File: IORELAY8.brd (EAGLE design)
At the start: 65 x 45 mm, 55 parts, among them Q1 2N7002, Q2 2N7002, Q3 2N7002, Q4 2N7002, Q5 2N7002, Q6 2N7002, Q7 2N7002, Q8 2N7002

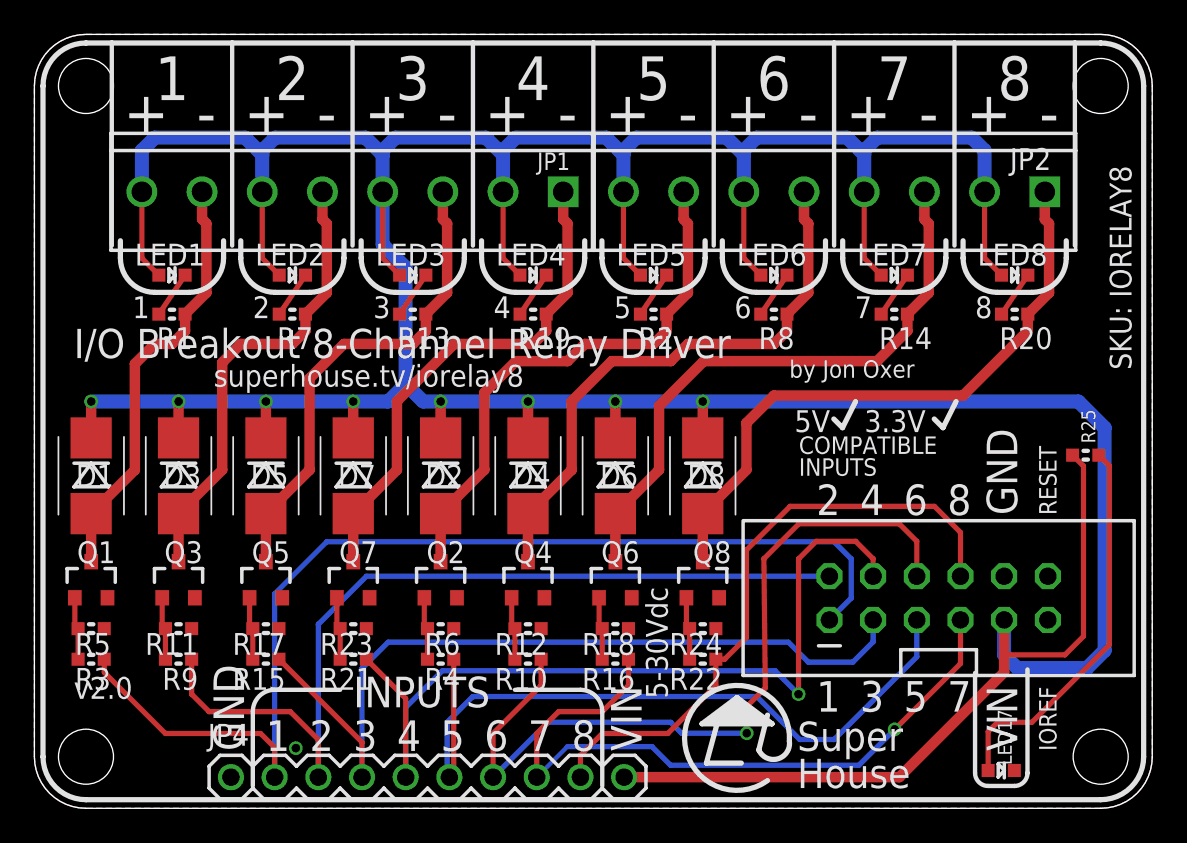
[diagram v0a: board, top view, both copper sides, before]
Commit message: Replaced most parts using SuperHouse library to add 3D models
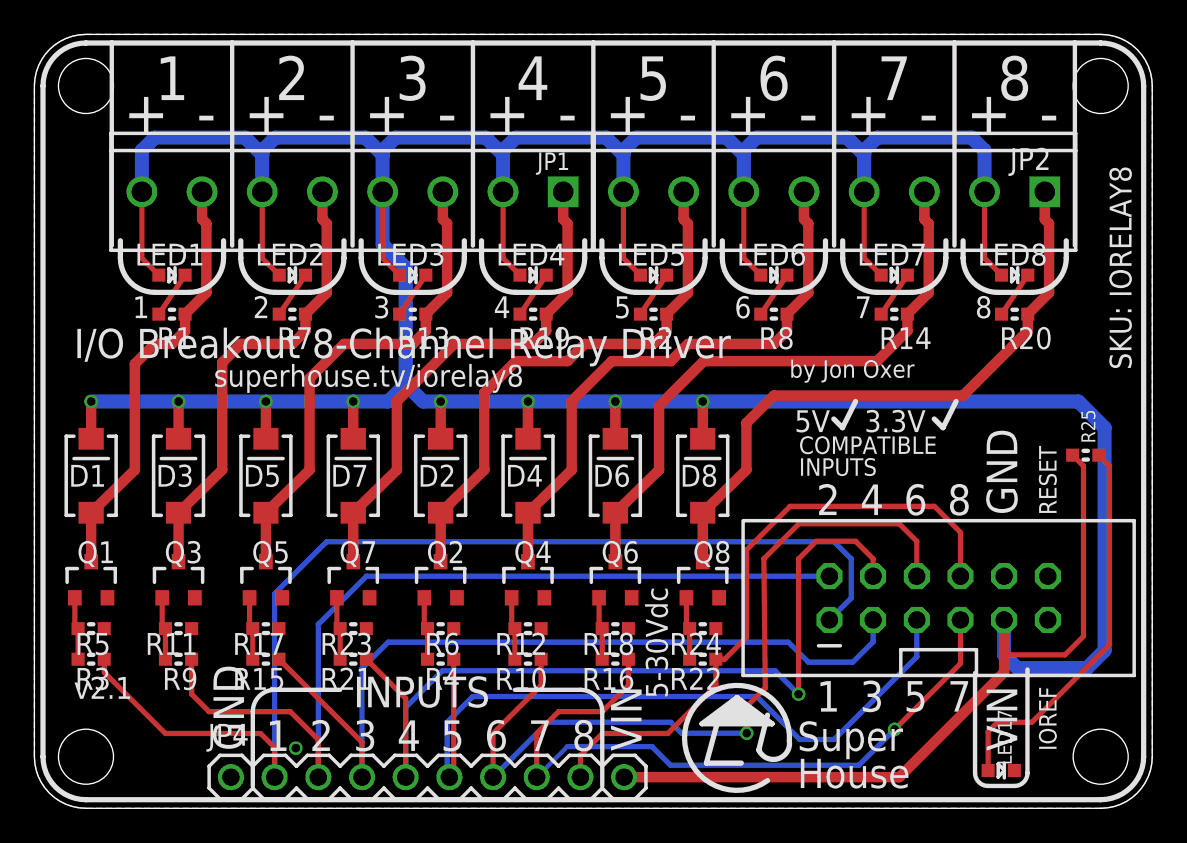
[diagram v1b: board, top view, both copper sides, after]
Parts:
- D1, D2, D3, D4, D5, D6, D7, D8: device freetronics-master-v1.1:SMB-DIODE -> SuperHouse-DiscreteSemi:SMA-DIODE
- JP4: value M100.1 -> M10-PLAIN; device freetronics-original:1X10 -> SuperHouse-Connectors:1X10
- LED1, LED17, LED2, LED3, LED4, LED5, LED6, LED7, LED8: device freetronics-master-v1:LED-0603 -> SuperHouse-LEDs:LED-0603
- Q1, Q2, Q3, Q4, Q5, Q6, Q7, Q8: device freetronics-master-v1:SOT23-3 -> SuperHouse-DiscreteSemi:SOT23-3
- R1, R10, R11, R12, R13, R14, R15, R16, R17, R18, R19, R2, R20, R21, R22, R23, R24, R25, R3, R4, R5, R6, R7, R8, R9: device freetronics-master-v1:0603 -> SuperHouse-DiscreteSemi:R0603
- turned D1 to 90 degrees
- turned D2 to 90 degrees
- turned D3 to 90 degrees
- turned D4 to 90 degrees
- turned D5 to 90 degrees
- turned D6 to 90 degrees
- turned D7 to 90 degrees
- turned D8 to 90 degrees
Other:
- board text added: "v2.1"
- board text removed: "v2.0"

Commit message: Replaced parts using SuperHouse libraries to add 3D models
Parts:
- JP1, JP2: value (none) -> M08-SCREW-3.5MM; device freetronics-master-v1:TERMINALBLOCK_3.5MM_8 -> SuperHouse-Connectors:SCREWTERMINAL_3.5MM_8
- JP3: value M06X2 -> M06X2-SHROUDED; device freetronics-jon:2X6-SHROUDED -> SuperHouse-Connectors:2X6-SHROUDED
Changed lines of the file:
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@@
 </layers>
 <board>
-<fusionsync huburn="a.cGVyc29uYWw6dWUyZDliZmNi" projecturn="a.cGVyc29uYWw6dWUyZDliZmNiIzIwMTkwNjE5MTk5NjgzNjgx" f3durn="urn:adsk.wipprod:dm.lineage:VjGxfGCsTMey9aZvXy2zdA" pcbguid="9329cc0c-2ea9-458a-91f7-0ed3767be766" lastpulledtime="" lastsyncedchangeguid="c08ba1bd-64e9-64fe-0de0-91ac47596278"/>
+<fusionsync huburn="a.cGVyc29uYWw6dWUyZDliZmNi" projecturn="a.cGVyc29uYWw6dWUyZDliZmNiIzIwMTkwNjE5MTk5NjgzNjgx" f3durn="urn:adsk.wipprod:dm.lineage:VjGxfGCsTMey9aZvXy2zdA" pcbguid="9329cc0c-2ea9-458a-91f7-0ed3767be766" lastpulledtime="" lastsyncedchangeguid="653f0fd4-dbab-250d-d7aa-35627fae340c"/>
 <plain>
 <wire x1="0" y1="3" x2="3" y2="0" width="0" layer="20" curve="90"/>
@@
 <attribute name="VALUE" x="59.166" y="21.1728" size="1.27" layer="27" font="vector"/>
 </element>
-<element name="JP1" library="freetronics-master-v1" package="TERMINALBLOCK_3.5MM_8" value="" x="30.75" y="35.846" smashed="yes" rot="R180">
+<element name="JP1" library="SuperHouse-Connectors" library_urn="urn:adsk.eagle:library:11765989" package="SCREWTERMINAL_3.5MM_8" package3d_urn="urn:adsk.eagle:package:12194855/2" value="M08-SCREW-3.5MM" x="30.75" y="35.846" smashed="yes" rot="R180">
 <attribute name="NAME" x="29.226" y="37.116" size="1.016" layer="25"/>
 <attribute name="VALUE" x="32.02" y="34.576" size="0.4064" layer="27" rot="R180"/>
 </element>
-<element name="JP2" library="freetronics-master-v1" package="TERMINALBLOCK_3.5MM_8" value="" x="58.75" y="35.846" smashed="yes" rot="R180">
+<element name="JP2" library="SuperHouse-Connectors" library_urn="urn:adsk.eagle:library:11765989" package="SCREWTERMINAL_3.5MM_8" package3d_urn="urn:adsk.eagle:package:12194855/2" value="M08-SCREW-3.5MM" x="58.75" y="35.846" smashed="yes" rot="R180">
 <attribute name="NAME" x="56.718" y="37.116" size="1.27" layer="25"/>
 <attribute name="VALUE" x="60.02" y="34.576" size="0.4064" layer="27" rot="R180"/>
 </element>
 <element name="U$6" library="OSHW" package="OSHW_10X200_NOTEXT" value="" x="15.24" y="27.337" smashed="yes" rot="MR0"/>
-<element name="JP3" library="freetronics-jon" package="2X6-SHROUDED" value="M06X2" x="46.228" y="10.954" smashed="yes" rot="R90">
+<element name="JP3" library="SuperHouse-Connectors" library_urn="urn:adsk.eagle:library:11765989" package="2X6-SHROUDED" package3d_urn="urn:adsk.eagle:package:11976015/2" value="M06X2-SHROUDED" x="46.228" y="10.954" smashed="yes" rot="R90">
 <attribute name="NAME" x="64.77" y="9.303" size="0.4064" layer="104" rot="R90"/>
 <attribute name="VALUE" x="40.894" y="9.303" size="0.4064" layer="27" font="vector" rot="R90"/>

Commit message: Silkscreen change for v2.2 release
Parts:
- R10, R13, R14, R15, R16, R9: value 1K -> 10K
- R17, R18, R23, R24, R5, R6: value 10K -> 1K
- moved R20 43.4 mm to (18.5, 8.67)
- moved R5 37.5 mm to (36.0, 28.7), turned to 0 degrees
- moved R7 35.0 mm to (50.0, 28.7)
- moved R14 28.1 mm to (28.7, 10.4), turned to 180 degrees
- moved R3 27.4 mm to (22.0, 28.7)
- moved R6 26.6 mm to (43.0, 28.7), turned to 0 degrees
- moved R18 25.5 mm to (8.38, 8.67), turned to 0 degrees
- moved R19 25.4 mm to (13.5, 8.67)
- moved R2 21.0 mm to (15.0, 28.7)
- moved R4 20.8 mm to (29.0, 28.7)
- moved R10 20.4 mm to (8.38, 10.4), turned to 180 degrees
- moved R15 20.4 mm to (33.8, 10.4), turned to 180 degrees
- moved R13 18.4 mm to (23.6, 10.4), turned to 180 degrees
- moved R23 15.3 mm to (33.8, 8.67), turned to 0 degrees
- moved D2 15.2 mm to (8.38, 19.3)
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- renumbered JP1 to J1, JP2 to J2, JP3 to J4, JP4 to J3
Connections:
- net D0: now also R17.2; no longer R3.2
- net D1: now also R18.2; no longer R9.2
- net D2: now also R19.2; no longer R15.2
- net D3: now also R20.2; no longer R21.2
- net D4: now also R21.2; no longer R4.2
- net D5: now also R22.2; no longer R10.2
- net D6: now also R23.2; no longer R16.2
- net D7: now also R24.2; no longer R22.2
- net GND: now also R10.1, R13.1, R14.1, R15.1, R16.1, R9.1; no longer R17.1, R18.1, R23.1, R24.1, R5.1, R6.1
- net N$1: now also R17.1, R9.2; no longer R3.1, R5.2
- net N$10: now also Q3.1, R11.2, R19.1; no longer Q5.1, R15.1, R17.2
- net N$11: now also D4.A, Q4.3, R4.2; no longer D7.A, Q7.3, R19.2
- net N$12: now also Q4.1, R12.2, R20.1; no longer Q7.1, R21.1, R23.2
- net N$13: now also D5.A, Q5.3, R5.2; no longer D2.A, Q2.3, R2.2
- net N$14: now also Q5.1, R13.2, R21.1; no longer Q2.1, R4.1, R6.2
- net N$15: now also D6.A, Q6.3, R6.2; no longer D4.A, Q4.3, R8.2
- net N$16: now also Q6.1, R14.2, R22.1; no longer Q4.1, R10.1, R12.2
- net N$17: now also D7.A, Q7.3, R7.2; no longer D6.A, Q6.3, R14.2
- net N$18: now also Q7.1, R15.2, R23.1; no longer Q6.1, R16.1, R18.2
- net N$19: now also R8.2; no longer R20.2
- net N$20: now also R16.2, R24.1; no longer R22.1, R24.2
- net N$21: now also R2.1; no longer R7.1
- net N$22: now also R4.1; no longer R19.1
- net N$23: now also R3.1; no longer R13.1
- net N$25: now also R5.1; no longer R2.1
- net N$26: now also R6.1; no longer R8.1
- net N$27: now also R7.1; no longer R14.1
- net N$28: now also R8.1; no longer R20.1
- net N$3: now also D2.A, Q2.3, R2.2; no longer D3.A, Q3.3, R7.2
- net N$8: now also Q2.1, R10.2, R18.1; no longer Q3.1, R11.2, R9.1
- net N$9: now also D3.A, Q3.3, R3.2; no longer D5.A, Q5.3, R13.2
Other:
- board text added: "(c)2017-2019 SuperHouse Automation"
- board text added: "v2.2"
- board text removed: "(c) 2017 SuperHouse Automation"
- board text removed: "v2.1"

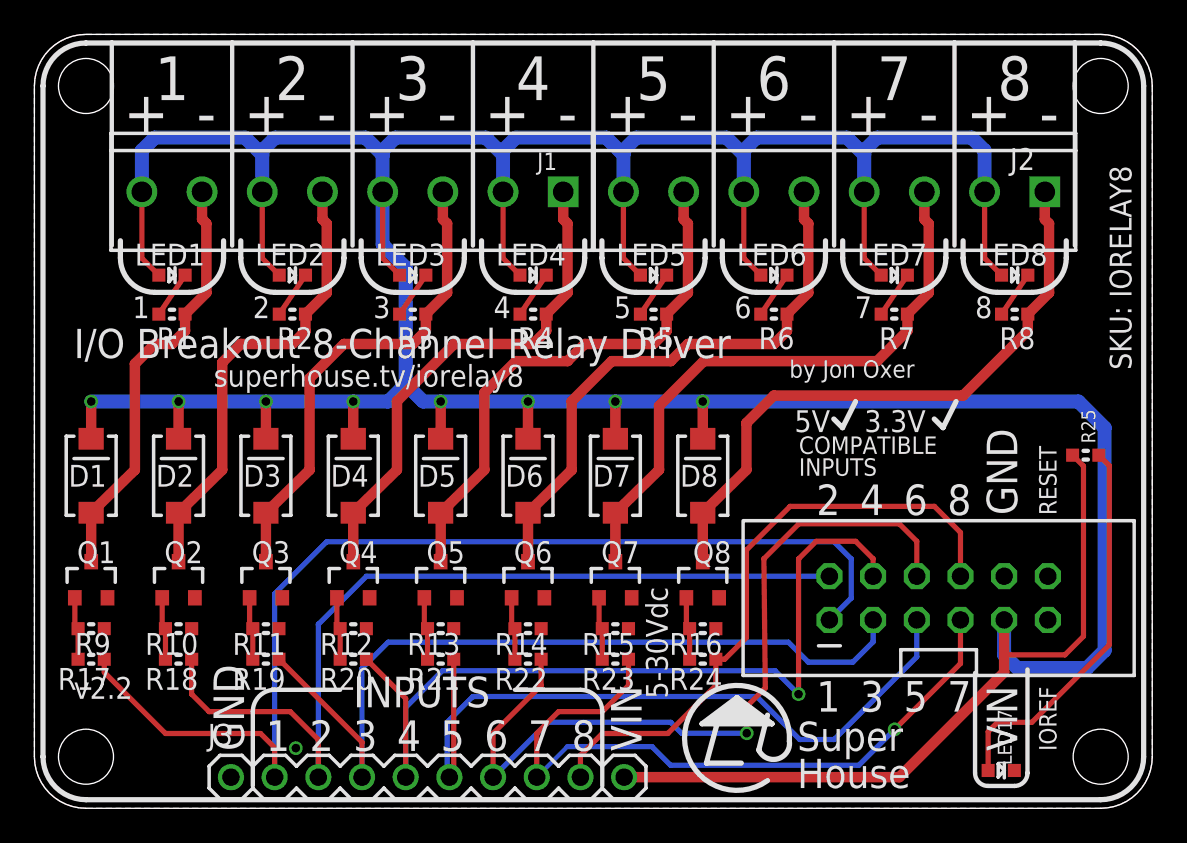
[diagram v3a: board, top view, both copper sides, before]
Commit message: DRC, designator, and value cleanups for v2.2 release
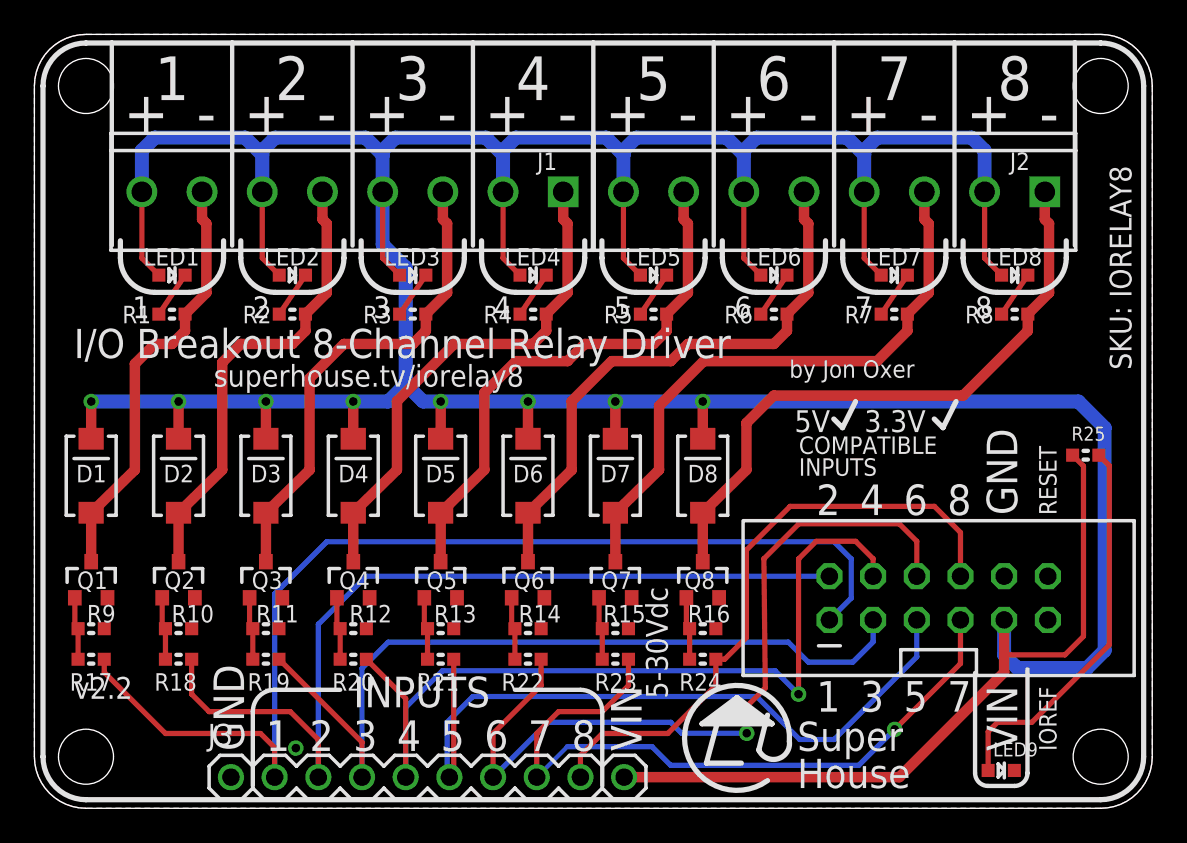
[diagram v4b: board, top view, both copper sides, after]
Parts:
- D1, D2, D3, D4, D5, D6, D7, D8: value 1N4004 SMB -> 1N4004 SMA
- renumbered LED17 to LED9
